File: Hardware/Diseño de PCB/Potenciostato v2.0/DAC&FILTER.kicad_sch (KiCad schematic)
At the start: 19 parts, among them IC4 MAX5217GUA+, IC5 MAX4477ASA+

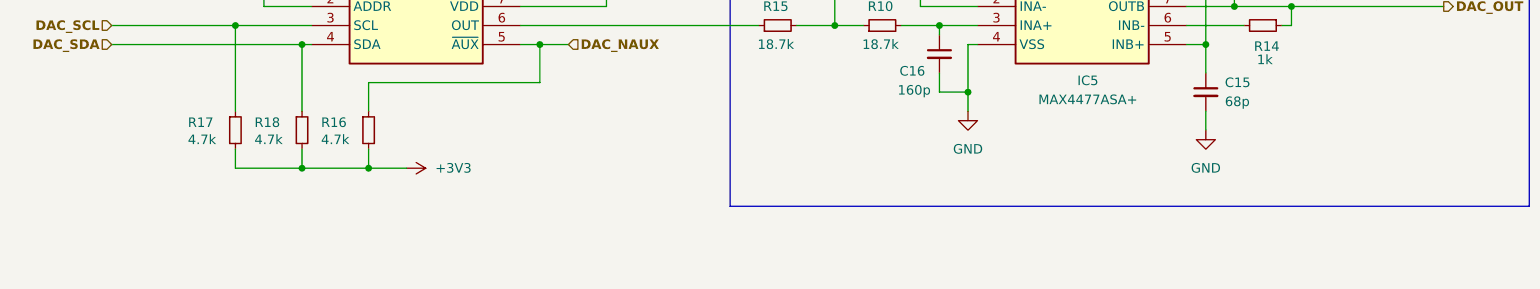
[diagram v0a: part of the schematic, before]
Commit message: Big commit. Hardware was already ready. Board arrived. Hardware testing phase and software development is ongoing, some hardware issues were detected and noted down in the KiCad project for future versions and design corrections. First software libraries under development for ADC, GPIO, Muxes and DAC managment (ADS1255, MAX5217, MAX4737, MAX4617 and GPIO)
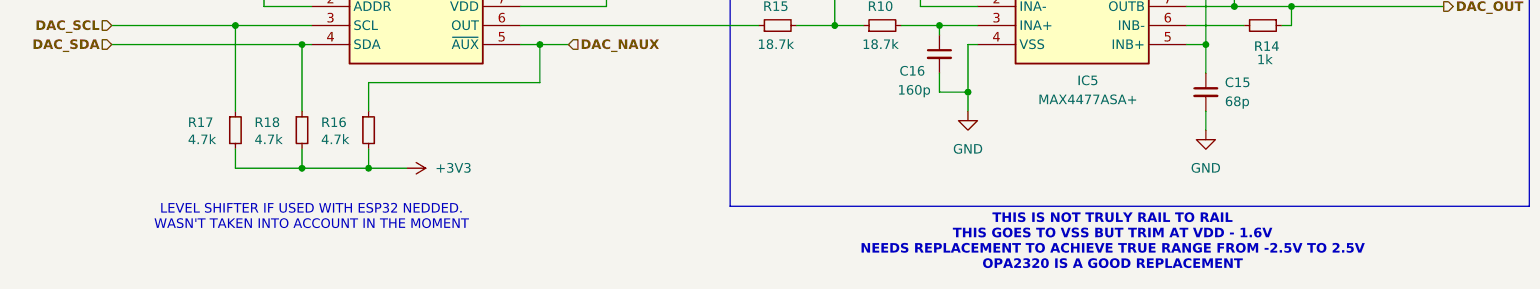
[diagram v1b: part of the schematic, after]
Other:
- note added: "LEVEL SHIFTER IF USED WITH ESP32 NEDDED. WASN'T TAKEN INTO ACCOUNT IN THE MOMENT"
- note added: "THIS IS NOT TRULY RAIL TO RAIL THIS GOES TO VSS BUT TRIM AT VDD - 1.6V NEEDS REPLACEMENT TO ACHIEVE TRUE RANGE FROM -2.5V TO 2.5V OPA2320 IS A GOOD REPLACEMENT"
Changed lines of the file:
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@@
+		)
+	)
+	(text "LEVEL SHIFTER IF USED WITH ESP32 NEDDED.\nWASN'T TAKEN INTO ACCOUNT IN THE MOMENT"
+		(exclude_from_sim no)
+		(at 86.36 122.174 0)
+		(effects
+			(font
+				(size 1.27 1.27)
+				(color 255 6 0 1)
+			)
+		)
+	)
+	(text "THIS IS NOT TRULY RAIL TO RAIL\nTHIS GOES TO VSS BUT TRIM AT VDD - 1.6V\nNEEDS REPLACEMENT TO ACHIEVE TRUE RANGE FROM -2.5V TO 2.5V\nOPA2320 IS A GOOD REPLACEMENT\n\n"
+		(exclude_from_sim no)
+		(at 193.294 126.492 0)
+		(effects
+			(font
+				(size 1.27 1.27)
+				(thickness 0.254)
+				(bold yes)
+				(color 255 0 6 1)
+			)
 		)
 	)

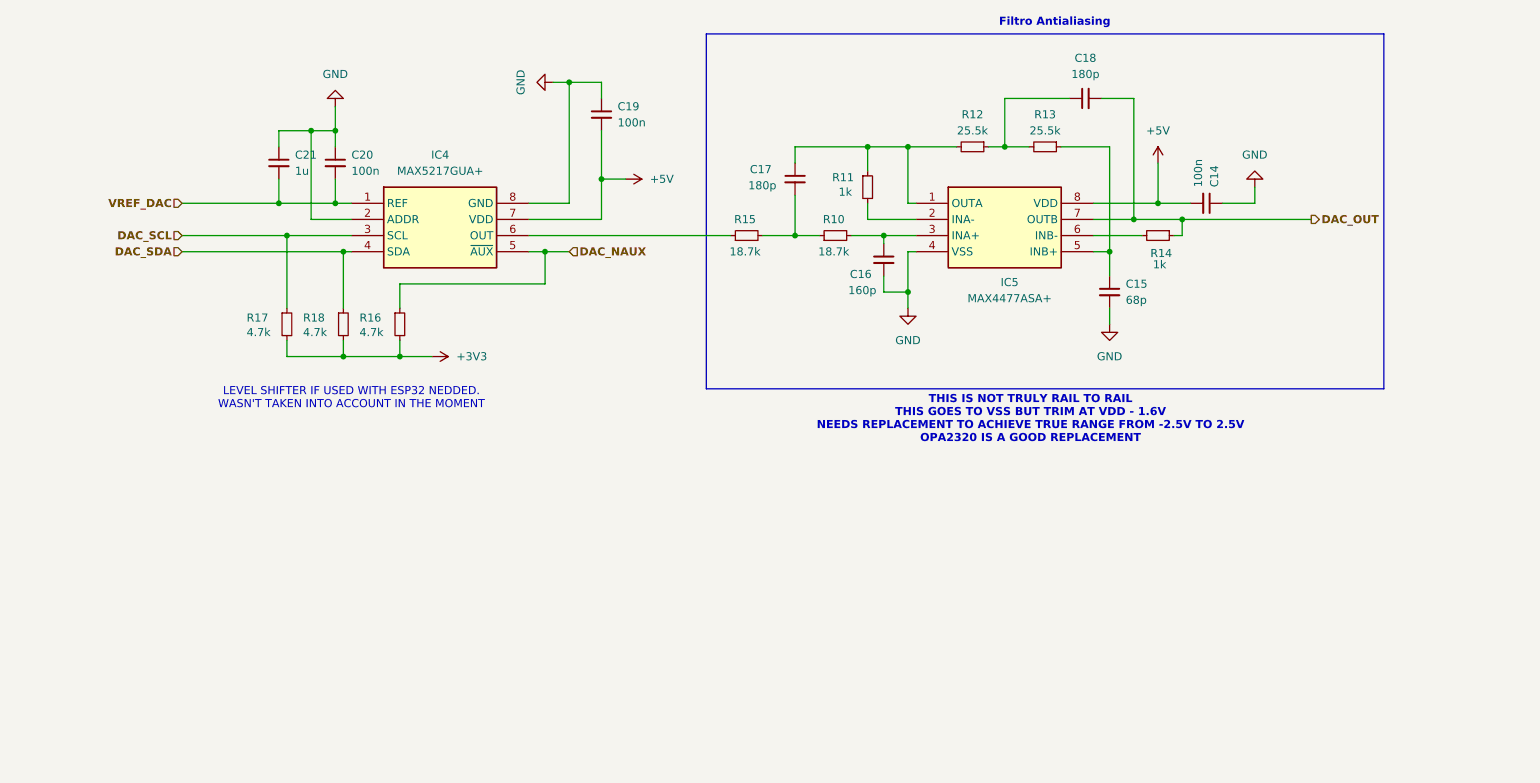
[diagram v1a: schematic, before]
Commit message: Hardware modifications. More notes added to the KiCad project related to hardware issues found during testing. USB Power and ground inverted corrected in design and PCB. MAX4477 replaced by OPA2320 in design and PCB. More notes with recommendations and advised can now be found in the schematics.
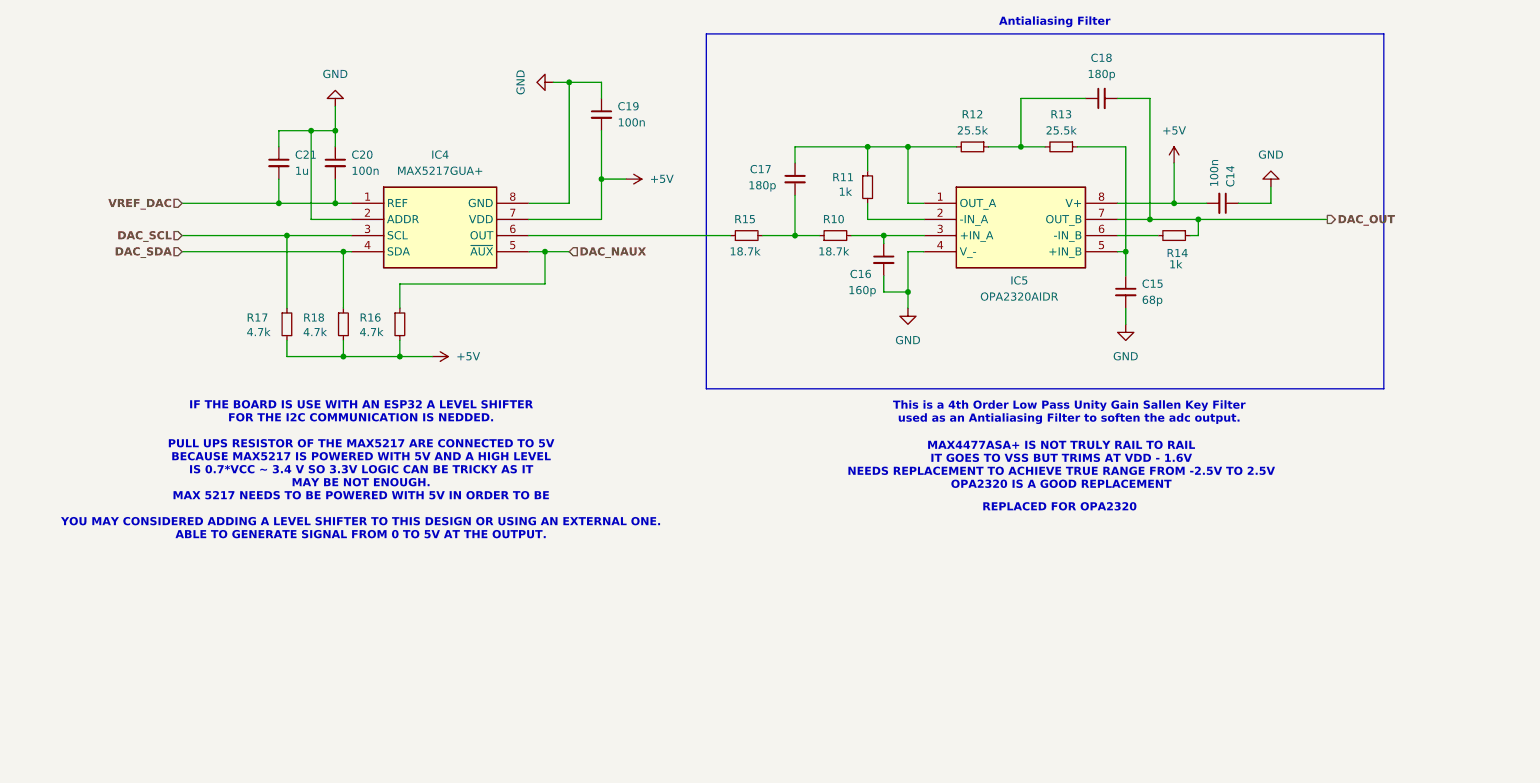
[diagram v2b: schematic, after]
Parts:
- removed IC5: MAX4477ASA+, potentiostat:SOIC127P600X175_MAX4477, symbol potentiostat:MAX4477ASA+
- added IC5: OPA2320AIDR, SOIC127P600X175-8N, symbol potentiostat:OPA2320AIDR
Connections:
- net +3V3 is gone; now on net +5V: R16.2, R17.2, R18.2
- net +5V: now also IC5.8 (V+)
- net DAC_OUT: now also IC5.7 (OUT_B)
- net GND: now also IC5.4 (V_-)
- net at C16.1, R10.2: now also IC5.3 (+IN_A)
- net at C17.1, R11.1, R12.2: now also IC5.1 (OUT_A)
- net at R14.2: now also IC5.6 (-IN_B)
- net at C15.1, R13.1: now also IC5.5 (+IN_B)
- net at R11.2: now also IC5.2 (-IN_A)
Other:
- note added: "Antialiasing Filter"
- note added: "IF THE BOARD IS USE WITH AN ESP32 A LEVEL SHIFTER FOR THE I2C COMMUNICATION IS NEDDED. PULL UPS RESISTOR OF THE MAX5217 ARE CONNECTED TO 5V BECAUSE MAX5217 IS POWERED WITH 5V AND A HIGH LEVEL IS 0.7*VCC ~ 3.4 V SO 3.3V LOGIC CAN BE TRICKY AS IT MAY BE NOT ENOUGH. MAX 5217 NEEDS TO BE POWERED WITH 5V IN ORDER TO BE YOU MAY CONSIDERED ADDING A LEVEL SHIFTER TO THIS DESIGN OR USING AN EXTERNAL ONE. 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"
- note added: "MAX4477ASA+ IS NOT TRULY RAIL TO RAIL IT GOES TO VSS BUT TRIMS AT VDD - 1.6V NEEDS REPLACEMENT TO ACHIEVE TRUE RANGE FROM -2.5V TO 2.5V OPA2320 IS A GOOD REPLACEMENT"
- note added: "REPLACED FOR OPA2320"
- note added: "This is a 4th Order Low Pass Unity Gain Sallen Key Filter used as an Antialiasing Filter to soften the adc output."
- note removed: "Filtro Antialiasing"
- note removed: "LEVEL SHIFTER IF USED WITH ESP32 NEDDED. WASN'T TAKEN INTO ACCOUNT IN THE MOMENT"
- note removed: "THIS IS NOT TRULY RAIL TO RAIL THIS GOES TO VSS BUT TRIM AT VDD - 1.6V NEEDS REPLACEMENT TO ACHIEVE TRUE RANGE FROM -2.5V TO 2.5V OPA2320 IS A GOOD REPLACEMENT"
- moved on the sheet: C14, C15, C18, R13, R14

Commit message: Further documentation and notes on the schematic. Software updates: In MAX4617, corrections in write function, more robust code verification to prevent overflows. In MUX, correction to MAX4617 gain codification and pinout updgraded for MAX4737. ADS1255, mux configured to AIN0-AINCOM in ADS_Initialized.
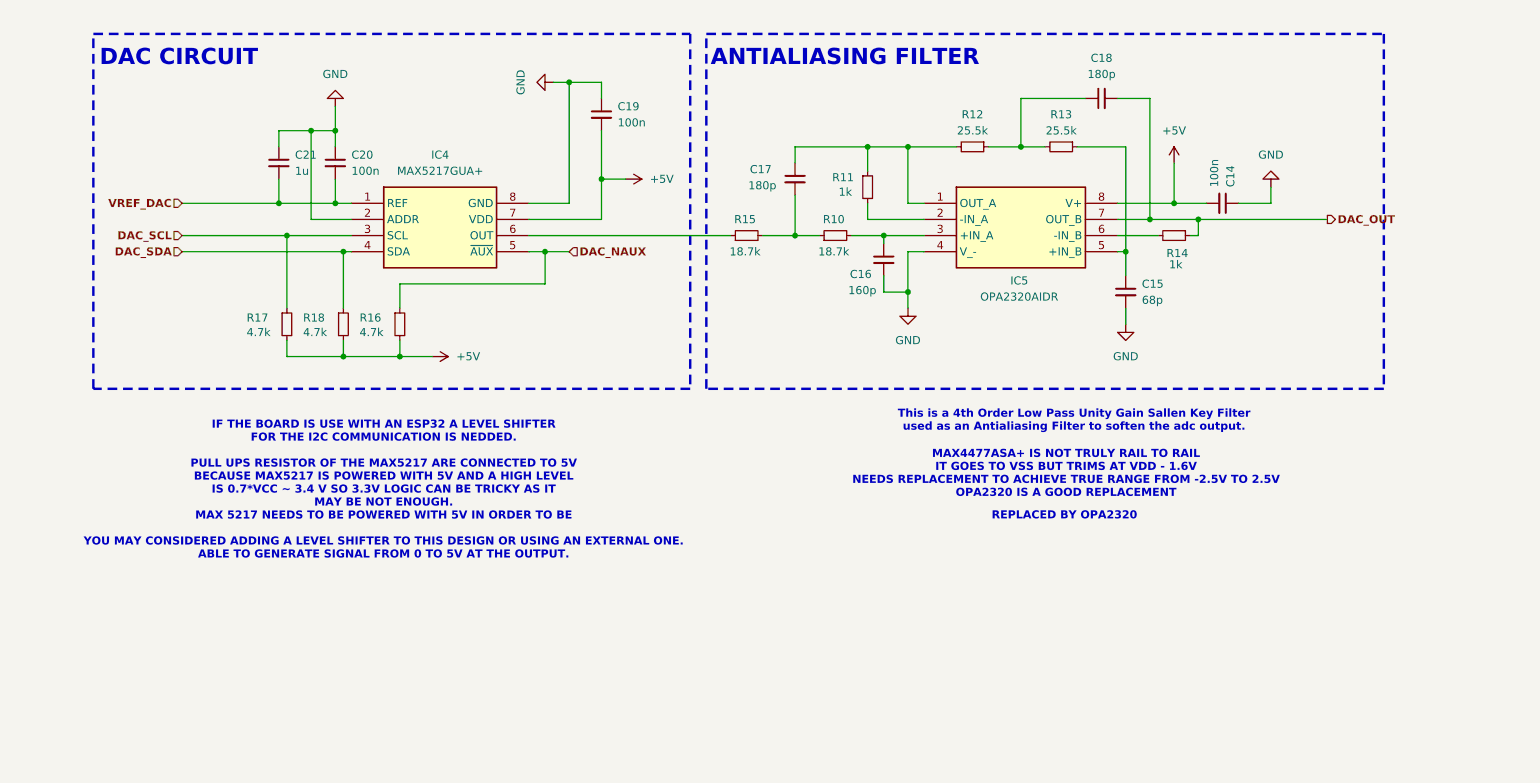
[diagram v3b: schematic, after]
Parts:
- IC5: Height 1.75 -> (none); Manufacturer_Part_Number OPA2320AIDR -> (none); Mouser Part Number 595-OPA2320AIDR -> (none); Mouser Price/Stock https://www.mouser.co.uk/ProductDetail/Texas-Instruments/OP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 -> (none)
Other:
- note added: "ANTIALIASING FILTER"
- note added: "DAC CIRCUIT"
- note added: "REPLACED BY OPA2320"
- note removed: "Antialiasing Filter"
- note removed: "REPLACED FOR OPA2320"
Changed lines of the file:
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@@
+	)
+	(rectangle
+		(start 45.72 64.77)
+		(end 139.7 120.65)
+		(stroke
+			(width 0.381)
+			(type dash)
+		)
+		(fill
+			(type none)
+		)
 	)
 	(rectangle
@@
 		(end 248.92 120.65)
 		(stroke
-			(width 0)
-			(type default)
+			(width 0.381)
+			(type dash)
 		)
 		(fill
@@
 	(text "IF THE BOARD IS USE WITH AN ESP32 A LEVEL SHIFTER \nFOR THE I2C COMMUNICATION IS NEDDED.\n\nPULL UPS RESISTOR OF THE MAX5217 ARE CONNECTED TO 5V\nBECAUSE MAX5217 IS POWERED WITH 5V AND A HIGH LEVEL\nIS 0.7*VCC ~ 3.4 V SO 3.3V LOGIC CAN BE TRICKY AS IT\nMAY BE NOT ENOUGH.\nMAX 5217 NEEDS TO BE POWERED WITH 5V IN ORDER TO BE\n\nYOU MAY CONSIDERED ADDING A LEVEL SHIFTER TO THIS DESIGN OR USING AN EXTERNAL ONE.\nABLE TO GENERATE SIGNAL FROM 0 TO 5V AT THE OUTPUT."
 		(exclude_from_sim no)
-		(at 87.884 133.604 0)
+		(at 91.44 136.652 0)
 		(effects
 			(font
@@
 		)
 	)
-	(text "REPLACED FOR OPA2320\n"
-		(exclude_from_sim no)
-		(at 197.866 139.446 0)
+	(text "ANTIALIASING FILTER\n"
+		(exclude_from_sim no)
+		(at 164.084 68.58 0)
+		(effects
+			(font
+				(size 2.54 2.54)
+				(thickness 0.508)
+				(bold yes)
+			)
+		)
+	)
+	(text "REPLACED BY OPA2320\n"
+		(exclude_from_sim no)
+		(at 198.628 140.716 0)
 		(effects
 			(font
@@
 	(text "MAX4477ASA+ IS NOT TRULY RAIL TO RAIL\nIT GOES TO VSS BUT TRIMS AT VDD - 1.6V\nNEEDS REPLACEMENT TO ACHIEVE TRUE RANGE FROM -2.5V TO 2.5V\nOPA2320 IS A GOOD REPLACEMENT\n\n"
 		(exclude_from_sim no)
-		(at 198.12 133.858 0)
+		(at 198.882 135.128 0)
 		(effects
 			(font
@@
 	(text "This is a 4th Order Low Pass Unity Gain Sallen Key Filter\nused as an Antialiasing Filter to soften the adc output."
 		(exclude_from_sim no)
-		(at 199.39 124.46 0)
+		(at 200.152 125.73 0)
 		(effects
 			(font
@@
 		)
 	)
-	(text "Antialiasing Filter\n"
-		(exclude_from_sim no)
-		(at 197.104 62.992 0)
+	(text "DAC CIRCUIT\n"
+		(exclude_from_sim no)
+		(at 59.182 68.58 0)
 		(effects
 			(font
-				(size 1.27 1.27)
-				(thickness 0.254)
+				(size 2.54 2.54)
+				(thickness 0.508)
 				(bold yes)
 			)
@@
 			)
 		)
-		(property "Height" "1.75"
-			(at 203.2 486.36 0)
-			(effects
-				(font
-					(size 1.27 1.27)
-				)
-				(justify left top)
-				(hide yes)
-			)
-		)
-		(property "Mouser Part Number" "595-OPA2320AIDR"
-			(at 203.2 586.36 0)
-			(effects
-				(font
-					(size 1.27 1.27)
-				)
-				(justify left top)
-				(hide yes)
-			)
-		)
-		(property "Mouser Price/Stock" "https://www.mouser.co.uk/ProductDetail/Texas-Instruments/OPA2320AIDR?qs=tTIQDc3uNmVIif8mgpifPg%3D%3D"
-			(at 203.2 686.36 0)
-			(effects
-				(font
-					(size 1.27 1.27)
-				)
-				(justify left top)
-				(hide yes)
-			)
-		)
 		(property "Manufacturer_Name" "Texas Instruments"
 			(at 203.2 786.36 0)
 			(effects
 				(font
-					(size 1.27 1.27)
-				)
-				(justify left top)
-				(hide yes)
-			)
-		)
-		(property "Manufacturer_Part_Number" "OPA2320AIDR"
-			(at 203.2 886.36 0)
-			(effects
-				(font

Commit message: Hardware: Hardware Corrections in Potentiostat, small but important ones (WE electrode, Normal Open connection for electric disconnection in schematic and PCB. DAC I2C pull up resistors connected to 5V PCB layout corrected.). New project for ESP32 board: board design to hold ESP32 and LevelShifter for I2C3.3V to 5V. No more. No big changes in firmware and software, nothing to note, really small corrections in that were in the way.
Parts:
- added U10: ~, symbol Graphics_images:UNS_logo
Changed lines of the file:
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@@
+	)
+	(symbol
+		(lib_id "Graphics_images:UNS_logo")
+		(at 238.76 166.37 0)
+		(unit 1)
+		(exclude_from_sim no)
+		(in_bom no)
+		(on_board no)
+		(dnp yes)
+		(fields_autoplaced yes)
+		(property "Reference" "U10"
+			(at 237.998 161.798 0)
+			(effects
+				(font
+					(size 1.27 1.27)
+				)
+				(justify left)
+				(hide yes)
+			)
+		)
+		(property "Value" "~"
+			(at 218.44 157.48 0)
+			(effects
+				(font
+					(size 1.27 1.27)
+				)
+				(justify left)
+			)
+		)
+		(property "Footprint" ""
+			(at 229.87 162.56 0)
+			(effects
+				(font
+					(size 1.27 1.27)
+				)
+				(hide yes)
+			)
+		)
+		(property "Datasheet" ""
+			(at 229.87 162.56 0)
+			(effects
+				(font
+					(size 1.27 1.27)
+				)
+				(hide yes)
+			)
+		)
+		(property "Description" ""
+			(at 229.87 162.56 0)
+			(effects
+				(font
+					(size 1.27 1.27)
+				)
+				(hide yes)
+			)
+		)
+		(property "JLCLIB" ""
+			(at 238.76 166.37 0)
+			(effects
+				(font
+					(size 1.27 1.27)
+				)
+				(hide yes)
+			)
+		)
+		(instances
+			(project "Potenciostato v2.0"
+				(path "/3273751a-bb69-4014-b380-866ff743e010/82e9cf1f-f335-4dd7-a310-2b4d96e27e89"
+					(reference "U10")
+					(unit 1)
+				)
+			)
+		)
 	)
 	(symbol
